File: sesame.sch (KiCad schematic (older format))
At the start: 155 parts, among them U1 ATmega32A-PU

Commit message: added rgb header
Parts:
- added J?: Conn_01x03_Female, symbol Connector:Conn_01x03_Female
- USB1: symbol Connector:USB_C_Receptacle_USB2.0 -> sesame-rescue:USB_C_Receptacle_USB2.0-Connector
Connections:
- net labels added: RGB
- wire segments 231 -> 234
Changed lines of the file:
@@
 	10150 5200 10250 5200
 $Comp
-L Connector:USB_C_Receptacle_USB2.0 USB1
+L sesame-rescue:USB_C_Receptacle_USB2.0-Connector USB1
 U 1 1 5F2A909F
 P 6450 5500
@@
 Text GLabel 10350 5950 2    50   Input ~ 0
 BOOT
+$Comp
+L Connector:Conn_01x03_Female J?
+U 1 1 600B7BCC
+P 10150 4150
+F 0 "J?" H 10178 4176 50  0000 L CNN
+F 1 "Conn_01x03_Female" H 10178 4085 50  0000 L CNN
+F 2 "" H 10150 4150 50  0001 C CNN
+F 3 "~" H 10150 4150 50  0001 C CNN
+	1    10150 4150
+	1    0    0    -1
+$EndComp
+$Comp
+L power:GND #PWR?
+U 1 1 600BA4D0
+P 9700 4250
+F 0 "#PWR?" H 9700 4000 50  0001 C CNN
+F 1 "GND" H 9705 4077 50  0000 C CNN
+F 2 "" H 9700 4250 50  0001 C CNN
+F 3 "" H 9700 4250 50  0001 C CNN
+	1    9700 4250
+	1    0    0    -1
+$EndComp
+$Comp
+L power:+5V #PWR?
+U 1 1 600BCA2C
+P 9700 4050
+F 0 "#PWR?" H 9700 3900 50  0001 C CNN
+F 1 "+5V" H 9715 4223 50  0000 C CNN
+F 2 "" H 9700 4050 50  0001 C CNN
+F 3 "" H 9700 4050 50  0001 C CNN
+	1    9700 4050
+	1    0    0    -1
+$EndComp
+Text GLabel 2300 5200 1    50   Input ~ 0
+RGB
+Text GLabel 9700 4150 0    50   Input ~ 0
+RGB
+Wire Wire Line
+	9950 4050 9700 4050
+Wire Wire Line
+	9950 4150 9700 4150
+Wire Wire Line
+	9950 4250 9700 4250
 $EndSCHEMATC

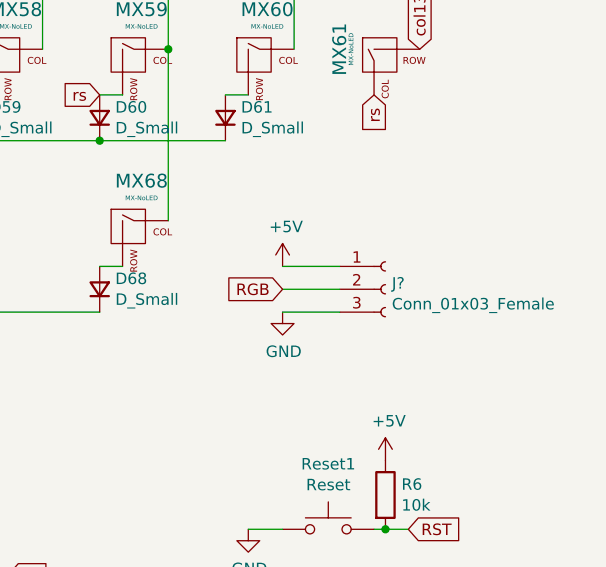
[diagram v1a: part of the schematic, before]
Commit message: add
-Double check implementation of Ws2812b(ex. caps for each led), (resistor between dataline and MCU pin)
-Add more more RGB LEDS to the schematic,  generate netlist
- OPen pcb view, read netlist, place the LEDs. Make sure on correct side. Then route traces
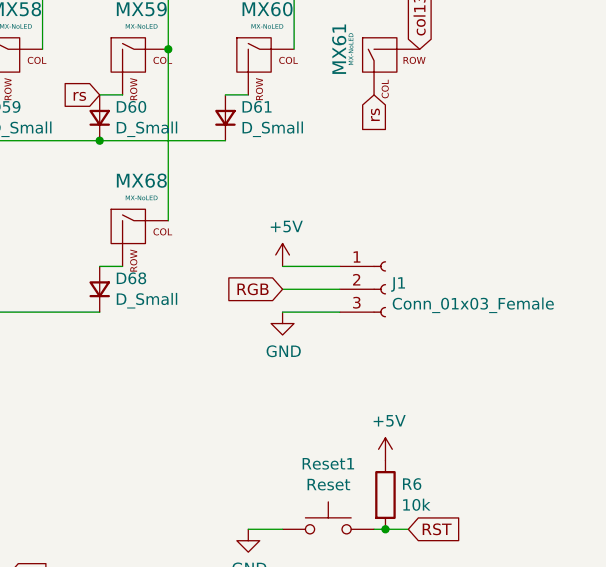
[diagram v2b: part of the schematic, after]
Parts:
- J1: renamed from J?; footprint (none) -> Connector_PinHeader_2.54mm:PinHeader_1x03_P2.54mm_Vertical
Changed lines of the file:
@@
 BOOT
 $Comp
-L Connector:Conn_01x03_Female J?
+L Connector:Conn_01x03_Female J1
 U 1 1 600B7BCC
 P 10150 4150
-F 0 "J?" H 10178 4176 50  0000 L CNN
+F 0 "J1" H 10178 4176 50  0000 L CNN
 F 1 "Conn_01x03_Female" H 10178 4085 50  0000 L CNN
-F 2 "" H 10150 4150 50  0001 C CNN
+F 2 "Connector_PinHeader_2.54mm:PinHeader_1x03_P2.54mm_Vertical" H 10150 4150 50  0001 C CNN
 F 3 "~" H 10150 4150 50  0001 C CNN
 	1    10150 4150
@@
 $EndComp
 $Comp
-L power:GND #PWR?
+L power:GND #PWR0103
 U 1 1 600BA4D0
 P 9700 4250
-F 0 "#PWR?" H 9700 4000 50  0001 C CNN
+F 0 "#PWR0103" H 9700 4000 50  0001 C CNN
 F 1 "GND" H 9705 4077 50  0000 C CNN
 F 2 "" H 9700 4250 50  0001 C CNN
@@
 $EndComp
 $Comp
-L power:+5V #PWR?
+L power:+5V #PWR0104
 U 1 1 600BCA2C
 P 9700 4050
-F 0 "#PWR?" H 9700 3900 50  0001 C CNN
+F 0 "#PWR0104" H 9700 3900 50  0001 C CNN
 F 1 "+5V" H 9715 4223 50  0000 C CNN
 F 2 "" H 9700 4050 50  0001 C CNN
